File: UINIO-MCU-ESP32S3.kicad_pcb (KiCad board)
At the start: 2 copper layers, 0 parts

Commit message: Complete schematic drawing.
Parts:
- added AE1: Antenna_Chip, RF_Antenna:Texas_SWRA117D_2.4GHz_Right, F.Cu at (197.5, 141.3)
- added C1: 1uF, Capacitor_SMD:C_0402_1005Metric, F.Cu at (131.2, 86.1)
- added C10: 10nF, Capacitor_SMD:C_0402_1005Metric, F.Cu at (139.0, 83.2)
- added C11: 0.1uF, Capacitor_SMD:C_0402_1005Metric, F.Cu at (131.2, 80.3)
- added C12: 0.1uF, Capacitor_SMD:C_0402_1005Metric, F.Cu at (133.1, 80.3)
- added C13: 0.1uF, Capacitor_SMD:C_0402_1005Metric, F.Cu at (135.1, 80.3)
- added C14: 0.1uF, Capacitor_SMD:C_0402_1005Metric, F.Cu at (137.1, 80.3)
- added C15: 15pF, Capacitor_SMD:C_0402_1005Metric, F.Cu at (139.0, 80.3)
- added C16: 15pF, Capacitor_SMD:C_0402_1005Metric, F.Cu at (131.2, 77.5)
- added C17: 1uF, Capacitor_SMD:C_0402_1005Metric, F.Cu at (133.1, 77.5)
- added C18: 0.1uF, Capacitor_SMD:C_0402_1005Metric, F.Cu at (135.1, 77.5)
- added C19: 0.1uF, Capacitor_SMD:C_0402_1005Metric, F.Cu at (137.1, 77.5)
- added C2: 1uF, Capacitor_SMD:C_0402_1005Metric, F.Cu at (133.1, 86.1)
- added C20: 1uF, Capacitor_SMD:C_0402_1005Metric, F.Cu at (139.0, 77.5)
- added C3: 0.1uF, Capacitor_SMD:C_0402_1005Metric, F.Cu at (135.1, 86.1)
- added C4: 1uF, Capacitor_SMD:C_0402_1005Metric, F.Cu at (137.1, 86.1)
- added C5: TBD, Capacitor_SMD:C_0402_1005Metric, F.Cu at (139.0, 86.1)
- added C6: 10uF, Capacitor_SMD:C_0402_1005Metric, F.Cu at (131.2, 83.2)
- added C7: 0.1uF, Capacitor_SMD:C_0402_1005Metric, F.Cu at (133.1, 83.2)
- added C8: TBD, Capacitor_SMD:C_0402_1005Metric, F.Cu at (135.1, 83.2)
- added C9: 1uF, Capacitor_SMD:C_0402_1005Metric, F.Cu at (137.1, 83.2)
- added D1: LED_Red, LED_SMD:LED_0603_1608Metric, F.Cu at (183.6, 83.5)
- added J1: Conn_01x03_Pin, Connector_PinHeader_2.54mm:PinHeader_1x03_P2.54mm_Vertical, F.Cu at (113.9, 159.2)
- added J2: Conn_01x27_Pin, Connector_PinHeader_2.54mm:PinHeader_1x27_P2.54mm_Vertical, F.Cu at (194.8, 132.3)
- added J3: Conn_01x04_Pin, Connector_PinHeader_2.54mm:PinHeader_1x04_P2.54mm_Vertical, F.Cu at (113.8, 132.4)
- added J4: Conn_01x27_Pin, Connector_PinHeader_2.54mm:PinHeader_1x27_P2.54mm_Vertical, F.Cu at (195.7, 159.3)
- added L1: TBD, Inductor_SMD:L_0402_1005Metric, F.Cu at (172.1, 90.7)
- added R1: 5.1K, Resistor_SMD:R_0402_1005Metric, F.Cu at (174.1, 90.7)
- added R2: 5.1K, Resistor_SMD:R_0402_1005Metric, F.Cu at (176.1, 90.7)
- added R3: 2K, Resistor_SMD:R_0402_1005Metric, F.Cu at (172.1, 87.8)
- added R4: 10K, Resistor_SMD:R_0402_1005Metric, F.Cu at (174.1, 87.8)
- added R5: 10K, Resistor_SMD:R_0402_1005Metric, F.Cu at (176.1, 87.8)
- added R6: 10K, Resistor_SMD:R_0402_1005Metric, F.Cu at (172.1, 84.9)
- added R7: 10K, Resistor_SMD:R_0402_1005Metric, F.Cu at (174.1, 84.9)
- added R8: 10K, Resistor_SMD:R_0402_1005Metric, F.Cu at (176.1, 84.9)
- added R9: 10K, Resistor_SMD:R_0402_1005Metric, F.Cu at (160.5, 49.2)
- added SW1: 复位, Uinio:KEY-SMD_4P-L4.2-W3.4-P2.15-LS4.7, F.Cu at (164.0, 111.6)
- added SW2: 启动选择, Uinio:KEY-SMD_4P-L4.2-W3.4-P2.15-LS4.7, F.Cu at (155.9, 112.6)
- added U1: ME6211C33M5G-N, Uinio:SOT-23-5_L3.0-W1.7-P0.95-LS2.8-BR, F.Cu at (125.7, 148.8)
- added U2: W25Q128JVSSIQ, Uinio:SOIC-8_L5.3-W5.3-P1.27-LS8.0-BL, F.Cu at (177.7, 145.9)
- added U3: ESP-PSRAM64H, Uinio:SOP-8_L4.9-W3.9-P1.27-LS6.0-BL, F.Cu at (143.1, 141.1)
- added U4: RS2227XUTQK10, Uinio:WQFN-10_L1.8-W1.4-P0.40-BL, F.Cu at (117.3, 143.1)
- added U5: ESP32-S3, Uinio:ESP32-S3, F.Cu at (158.3, 145.2)
- added U6: CH343P, Uinio:TQFN-16_L3.0-W3.0-P0.50-BL-EP1.7, F.Cu at (179.5, 83.1)
- added U7: LMBT3904DW1T1G, Uinio:SOT-363_L2.0-W1.3-P0.65-LS2.1-TL, F.Cu at (142.3, 126.7)
- added USB1: USB_Type_C_16Pin, Uinio:USB-C-SMD_TYPEC-304J-BCP16, F.Cu at (103.5, 145.1)
- added Y1: 40MHz, Crystal:Crystal_SMD_3225-4Pin_3.2x2.5mm, F.Cu at (187.6, 89.5)

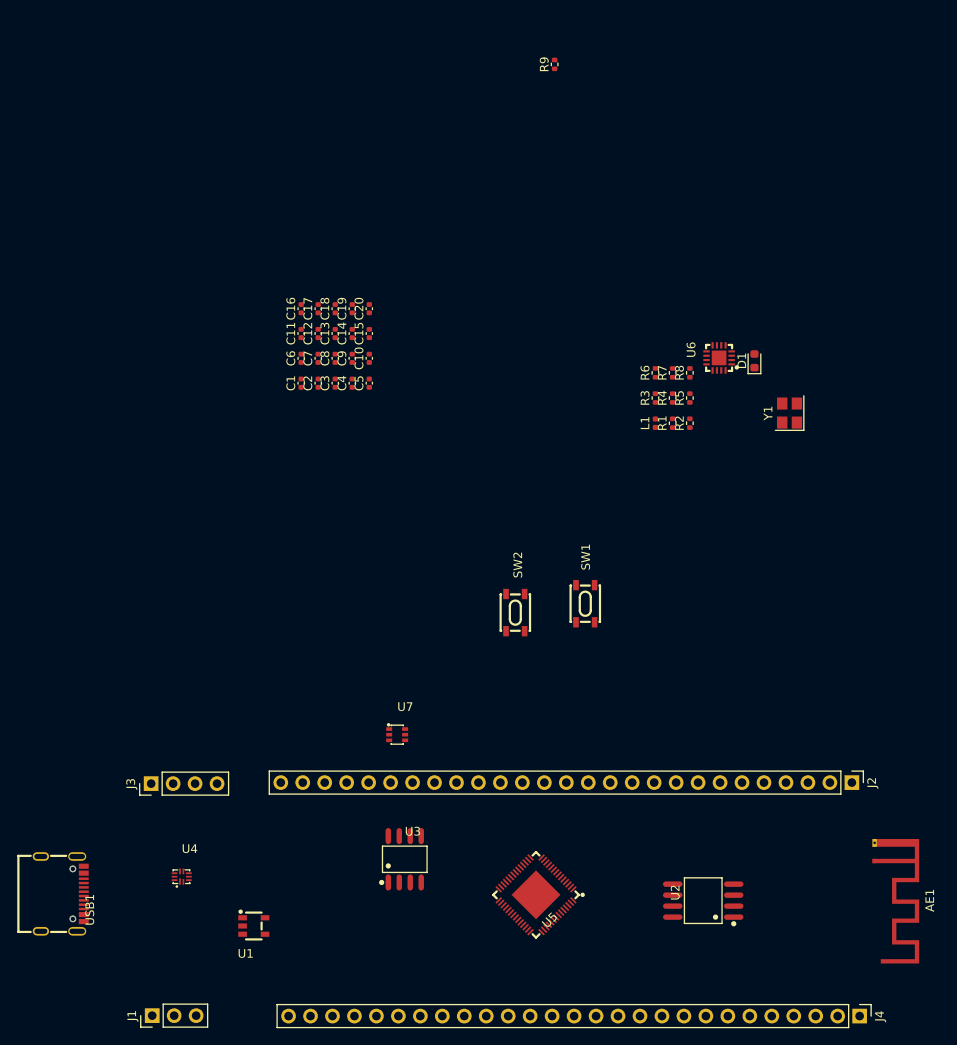
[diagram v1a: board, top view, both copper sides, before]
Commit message: PCB layout finish.
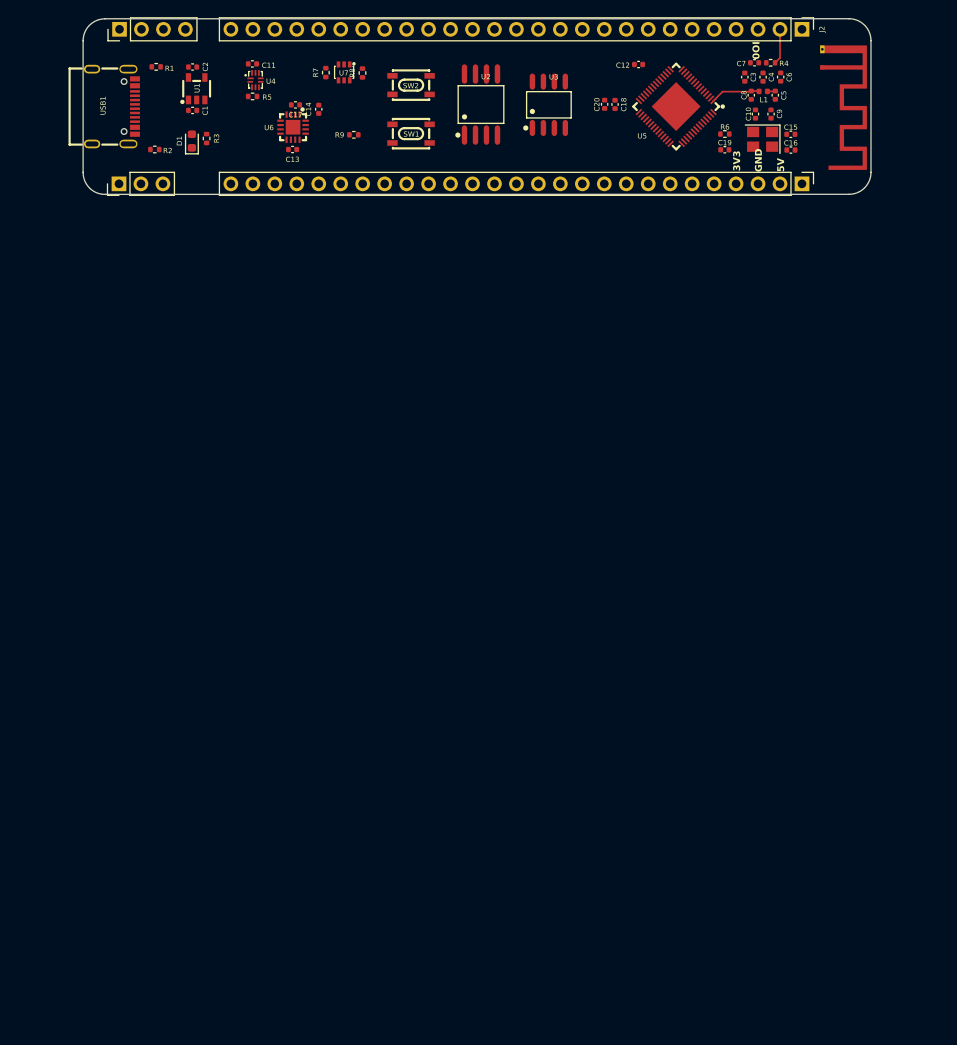
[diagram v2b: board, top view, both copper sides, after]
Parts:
- moved U1 97.0 mm to (119.1, 52.0), turned to -90 degrees
- moved J4 96.5 mm to (189.1, 63.0)
- moved J1 96.3 mm to (110.1, 63.0)
- moved U2 95.6 mm to (151.9, 53.9), turned to 0 degrees
- moved U5 92.6 mm to (174.5, 54.1)
- moved U4 92.5 mm to (125.9, 51.0), turned to -90 degrees
- moved AE1 92.0 mm to (191.4, 49.6)
- moved USB1 91.2 mm to (109.5, 54.1)
- moved U3 88.8 mm to (159.8, 53.9)
- moved J3 87.3 mm to (110.2, 45.1)
- moved J2 87.3 mm to (189.1, 45.1)
- moved U7 76.8 mm to (136.1, 50.1), turned to -90 degrees
- moved R1 72.6 mm to (114.4, 49.5), turned to 0 degrees
- moved D1 69.8 mm to (118.5, 58.1)
- moved R2 69.5 mm to (114.2, 59.0), turned to 0 degrees
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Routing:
- net Net-(U5-LNA_IN): track 0.00 -> 5.78 mm
- net /VDD_3.3V: track 0.00 -> 4.11 mm
- net Net-(AE1-FEED): track 0.00 -> 0.92 mm
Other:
- board outline added: 91.1 x 20.3 mm
- board text added: "3V3"
- board text added: "5V"
- board text added: "GND"
- board text added: "IO0"

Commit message: Update PCB layout.
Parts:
- added ?: LOGO, LOGO, F.Cu at (115.5, 54.3)
- added HOLE**: Hole-1mm, Uinio:Hole-1mm, F.Cu at (191.9, 62.9)
- added HOLE**: Hole-1mm, Uinio:Hole-1mm, F.Cu at (120.3, 62.7)
- added HOLE**: Hole-1mm, Uinio:Hole-1mm, F.Cu at (120.3, 45.3)
- added HOLE**: Hole-1mm, Uinio:Hole-1mm, F.Cu at (191.9, 45.1)
- moved R8 11.4 mm to (126.8, 51.1)
- moved U7 11.3 mm to (124.9, 51.5)
- moved R7 11.1 mm to (123.0, 51.1)
- moved R9 7.56 mm to (133.7, 50.7)
- moved C12 7.09 mm to (163.3, 51.1)
- moved C11 5.21 mm to (125.2, 54.4)
- moved U4 5.19 mm to (125.2, 56.2)
- moved R5 5.10 mm to (125.2, 58.0)
- moved R2 4.33 mm to (118.5, 59.6)
- moved C20 4.25 mm to (162.0, 54.0)
- moved R1 4.17 mm to (118.5, 48.9)
- moved C18 4.15 mm to (163.3, 54.0)
- moved U3 3.90 mm to (155.9, 54.1)
- moved C14 3.85 mm to (129.5, 55.4), turned to 0 degrees
- moved C10 3.74 mm to (180.1, 54.0), turned to 90 degrees
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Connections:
- J4 pad 10: /GPIO39 -> /GPIO36
- J4 pad 11: /GPIO38 -> /GPIO37
- J4 pad 12: /GPIO33 -> /GPIO35
- J4 pad 14: /GPIO35 -> /GPIO33
- J4 pad 15: /GPIO36 -> /SPICLK_P/GPIO47
- J4 pad 16: /GPIO37 -> /SPICLK_N/GPIO48
- J4 pad 17: /SPICLK_P/GPIO47 -> /SPID/GPIO32
- J4 pad 18: /SPICLK_N/GPIO48 -> /SPIQ/GPIO31
- J4 pad 19: /SPID/GPIO32 -> /SPICLK/GPIO30
- J4 pad 2: /VDD_5V -> /VDD_3.3V
- J4 pad 20: /SPIQ/GPIO31 -> /SPICS0/GPIO29
- J4 pad 21: /SPICLK/GPIO30 -> /SPIWP/GPIO28
- J4 pad 22: /SPICS0/GPIO29 -> /SPIHD/GPIO27
- J4 pad 23: /SPIWP/GPIO28 -> /VDD_SPI/GPIO11
- J4 pad 24: /SPIHD/GPIO27 -> /VDD_3.3V
- J4 pad 25: /VDD_SPI/GPIO11 -> GND
- J4 pad 26: /VDD_3.3V -> /VDD_5V
- J4 pad 3: GND -> /GPIO46
- J4 pad 4: /VDD_3.3V -> /GPIO45
- J4 pad 5: /GPIO46 -> /GPIO42
- J4 pad 6: /GPIO45 -> /GPIO41
- J4 pad 7: /GPIO42 -> /GPIO40
- J4 pad 8: /GPIO41 -> /GPIO39
- J4 pad 9: /GPIO40 -> /GPIO38
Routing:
- net /SPIWP/GPIO28: track 0.00 -> 36.7 mm
- net /SPICLK/GPIO30: track 0.00 -> 27.6 mm
- net /SPIQ/GPIO31: track 0.00 -> 25.3 mm
- net /SPID/GPIO32: track 0.00 -> 22.9 mm
- net /SPICLK_N/GPIO48: track 0.00 -> 20.5 mm
- net /SPICLK_P/GPIO47: track 0.00 -> 18.1 mm
- net /SPICS0/GPIO29: track 0.00 -> 17.8 mm
- net /GPIO33: track 0.00 -> 15.8 mm
- net /GPIO34: track 0.00 -> 13.4 mm
- net /GPIO35: track 0.00 -> 11.0 mm
- net Net-(U5-XTAL_P): track 0.00 -> 8.91 mm
- net /GPIO37: track 0.00 -> 8.64 mm
- net Net-(U5-XTAL_N): track 0.00 -> 6.86 mm
- net /GPIO36: track 0.00 -> 6.33 mm
- net Net-(U5-LNA_IN): track 5.78 -> 10.0 mm
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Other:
- board text added: "BOOT"
- board text added: "DTR"
- board text added: "ESP32-S3"
- board text added: "Flash"
- board text added: "IO1"
- board text added: "IO10"
- board text added: "IO11"
- board text added: "IO12"
- board text added: "IO13"
- board text added: "IO14"
- board text added: "IO15"
- board text added: "IO16"
- board text added: "IO17"
- board text added: "IO18"
- board text added: "IO19"
- board text added: "IO2"
- board text added: "IO20"
- board text added: "IO21"
- board text added: "IO26"
- board text added: "IO27"
- board text added: "IO28"
- board text added: "IO29"
- board text added: "IO3"
- board text added: "IO30"
- board text added: "IO31"
- board text added: "IO32"
- board text added: "IO33"
- board text added: "IO34"
- board text added: "IO35"
- board text added: "IO36"
- board text added: "IO37"
- board text added: "IO39"
- board text added: "IO4"
- board text added: "IO40"
- board text added: "IO41"
- board text added: "IO42"
- board text added: "IO45"
- board text added: "IO46"
- board text added: "IO47"
- board text added: "IO48"
- board text added: "IO5"
- board text added: "IO6"
- board text added: "IO7"
- board text added: "IO8"
- board text added: "IO9"
- board text added: "PSRAM"
- board text added: "REST"
- board text added: "RTS"
- board text added: "RXD"
- board text added: "TXD"
- board text added: "UART"
- board text added: "USB"
- board text added: "⇆"
- board text added: "下载方式"

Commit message: Start wiring.
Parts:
- moved C12 4.17 mm to (167.3, 49.8)
- moved C5 1.55 mm to (188.1, 52.4), turned to 90 degrees
- moved C8 1.35 mm to (185.3, 53.3)
- moved L1 1.35 mm to (186.7, 52.9)
- moved R5 1.21 mm to (124.1, 58.5)
- moved C11 1.12 mm to (124.1, 54.3)
- moved U4 1.12 mm to (124.1, 56.2)
- moved R9 1.03 mm to (132.7, 50.4)
- moved R6 0.76 mm to (177.6, 57.7)
- moved C17 0.60 mm to (132.7, 52.3)
- moved C19 0.60 mm to (176.4, 57.8), turned to 90 degrees
- moved C6 0.46 mm to (183.8, 51.4)
- moved HOLE** 0.43 mm to (191.5, 45.3)
- moved HOLE** 0.42 mm to (191.5, 62.9)
- moved R8 0.41 mm to (126.6, 51.4)
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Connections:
- J3 pad 2: /U0RXD -> /U0TXD
- J3 pad 3: /U0TXD -> /U0RXD
- J4 pad 10: /GPIO36 -> /GPIO37
- J4 pad 11: /GPIO37 -> /GPIO36
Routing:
- net /U0RXD: track 0.00 -> 74.6 mm, vias 0 -> 2
- net /U0TXD: track 0.00 -> 74.4 mm, vias 0 -> 2
- net /VDD_SPI/GPIO11: track 0.00 -> 59.4 mm, vias 0 -> 4
- net /CHIP_PU: track 0.00 -> 57.1 mm, vias 0 -> 2
- net /VDD_3.3V: track 0.00 -> 56.8 mm, vias 0 -> 2
- net /GPIO19/ESP32_USB_D-: track 0.00 -> 53.4 mm, vias 0 -> 1
- net /GPIO20/ESP32_USB_D+: track 0.00 -> 53.1 mm, vias 0 -> 1
- net /SPIHD/GPIO27: track 0.00 -> 46.0 mm, vias 0 -> 2
- net /SPICS1/GPIO26: track 0.00 -> 43.5 mm, vias 0 -> 1
- net /GPIO21: track 0.00 -> 39.8 mm
- net GND: track 0.00 -> 36.1 mm, vias 0 -> 1
- net /GPIO0: track 0.00 -> 35.5 mm
- net /GPIO18: track 0.00 -> 32.7 mm
- net /GPIO17: track 0.00 -> 30.3 mm
- net /VDD_5V: track 0.00 -> 29.5 mm, vias 0 -> 3
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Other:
- board text added: "下载选择"
- board text removed: "下载方式"

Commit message: Start wiring.
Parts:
- moved U3 1.40 mm to (157.5, 54.1)
- moved C20 0.88 mm to (162.8, 54.1)
- moved U2 0.79 mm to (149.4, 54.1)
- moved C18 0.75 mm to (164.0, 54.1)
- moved SW2 0.37 mm to (141.4, 51.5)
- moved SW1 0.35 mm to (141.4, 56.6)
- moved C17 0.09 mm to (132.8, 52.2)
- moved U6 0.07 mm to (132.5, 55.7)
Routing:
- net /SPIWP/GPIO28: track 44.1 -> 45.1 mm
- net /SPIHD/GPIO27: track 46.0 -> 47.1 mm
- net /SPIQ/GPIO31: track 36.6 -> 37.1 mm

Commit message: Start wiring.
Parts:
- J2, J4: moved to B.Cu
- turned J2 to 90 degrees
- turned J4 to 90 degrees

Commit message: Start wiring.
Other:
- board text added: "可选"
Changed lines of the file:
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@@
+    (effects (font (size 0.8 0.8) (thickness 0.1)) (justify left bottom))
+  )
+  (gr_text "可选" (at 135.56 54.11 90) (layer "F.SilkS")
     (effects (font (size 0.8 0.8) (thickness 0.1)) (justify left bottom))
   )

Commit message: Start wiring.
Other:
- board text added: "可选装"
- board text removed: "可选"
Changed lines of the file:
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@@
     (property "uuid" "std:7d19d6f006684f60afb0c218c16ed1d9")
     (attr through_hole)
-    (fp_text reference "U6" (at -3.092055 -1.354337 unlocked) (layer "F.SilkS")
+    (fp_text reference "U6" (at -2.69 -0.434337 90 unlocked) (layer "F.SilkS")
         (effects (font (size 0.6 0.6) (thickness 0.1)) (justify right))
     )
@@
     (effects (font (size 0.8 0.8) (thickness 0.1)) (justify left bottom))
   )
-  (gr_text "可选" (at 135.56 54.11 90) (layer "F.SilkS")
+  (gr_text "可选装" (at 135.76 55.22 90) (layer "F.SilkS")
     (effects (font (size 0.8 0.8) (thickness 0.1)) (justify left bottom))
   )
